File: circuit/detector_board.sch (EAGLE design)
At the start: 10 parts

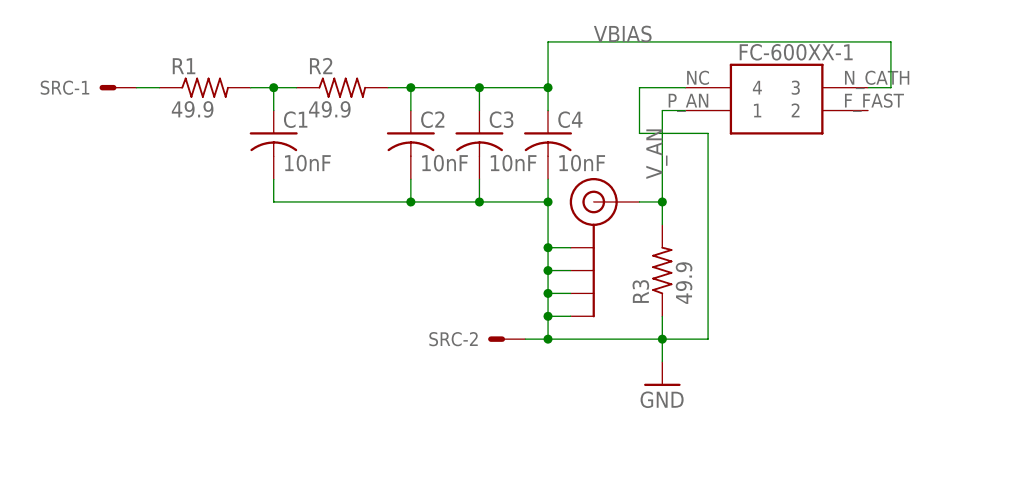
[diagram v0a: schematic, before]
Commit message: Modified board. Tried to add Spice model.
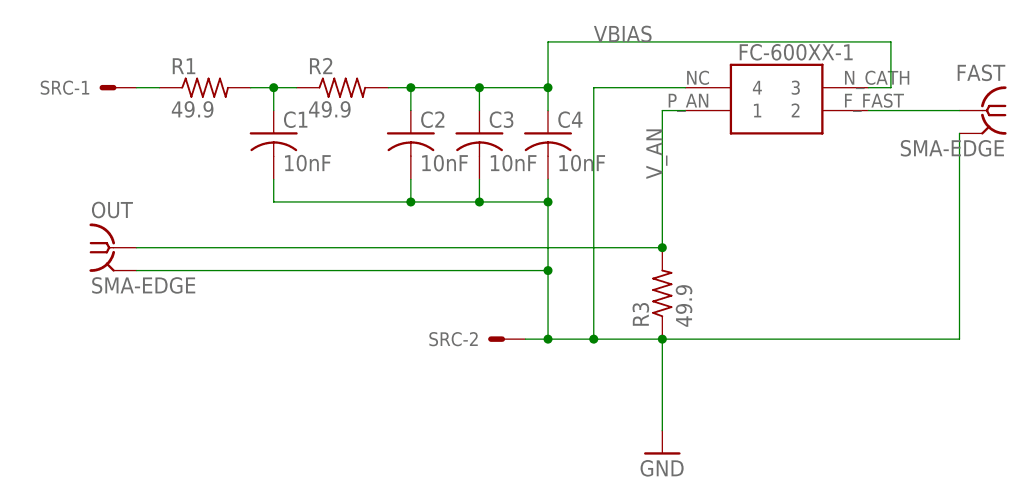
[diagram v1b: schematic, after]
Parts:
- removed J$1: SMA_EDGE, SparkFun-Retired:SMA_EDGE
- added FAST, OUT: SMA-EDGE, 000phys605parts:SMA-EDGE
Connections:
- new net N$2: FAST.1, FC-600XX-1.2
- net GND: now also FAST.2, OUT.2; no longer J$1.GND@0, J$1.GND@1, J$1.GND@2, J$1.GND@3
- net V_AN: now also OUT.1; no longer J$1.SIGNAL
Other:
- moved on the sheet: R3
